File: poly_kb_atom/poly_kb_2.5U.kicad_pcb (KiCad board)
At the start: 2 copper layers, 47.6 x 19 mm, 46 parts, among them J1 Conn_01x16, J10 North2, J2 North, J3 WestFront, J4 EastFront, J5 WestBack, J6 EastBack, J7 South, J8 North2, J9 South2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

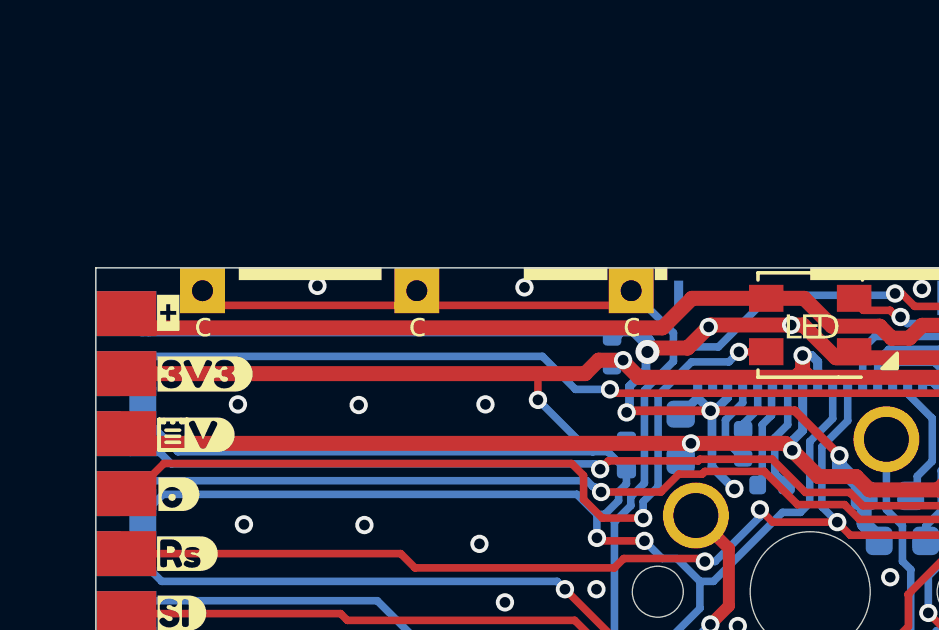
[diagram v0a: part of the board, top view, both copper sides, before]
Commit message: Added optional C7 and fix LED silkscreens
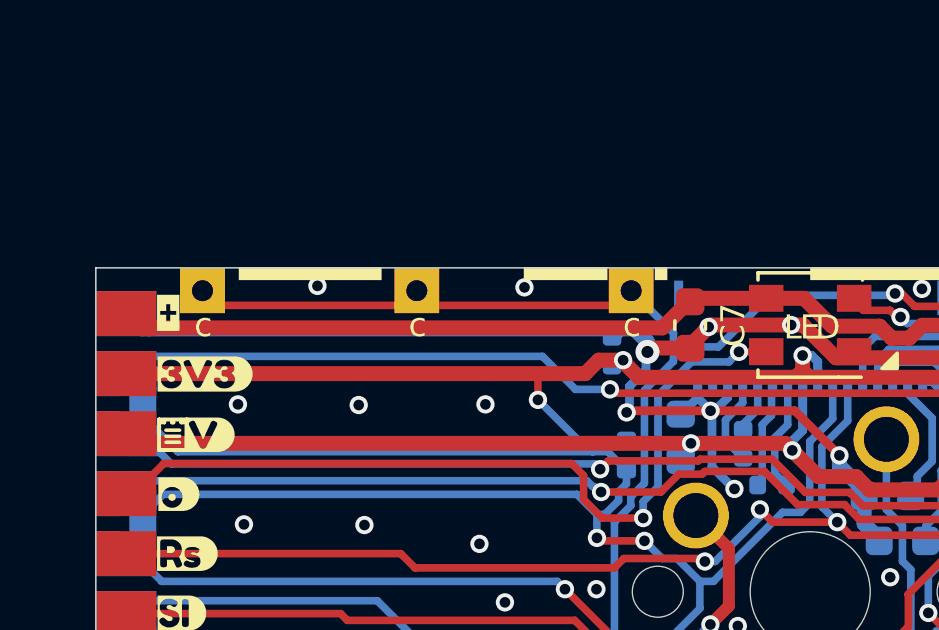
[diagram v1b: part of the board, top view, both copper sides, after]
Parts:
- removed the J10 at (81.5, 54.9)
- added C7: 100nF, Capacitor_SMD:C_0603_1608Metric, F.Cu at (97.7, 56.1)
- added J11: North2, poly_kb:TestPoin_1.5x1.5mm_Drill0.7mm, F.Cu at (81.5, 54.9)
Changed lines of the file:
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@@
       ) (layer "F.SilkS") (width 0) (fill solid))
+  )
+  (footprint "Capacitor_SMD:C_0603_1608Metric" (layer "F.Cu")
+    (at 97.7265 56.0578 -90)
+    (descr "Capacitor SMD 0603 (1608 Metric), square (rectangular) end terminal, IPC_7351 nominal, (Body size source: IPC-SM-782 page 76, https://www.pcb-3d.com/wordpress/wp-content/uploads/ipc-sm-782a_amendment_1_and_2.pdf), generated with kicad-footprint-generator")
+    (tags "capacitor")
+    (property "LCSC" "C19666")
+    (property "Sheetfile" "SSD1306_TO_SPI.kicad_sch")
+    (property "Sheetname" "sheet605ED2EB")
+    (attr smd)
+    (fp_text reference "C7" (at 0 -1.43 90) (layer "F.SilkS")
+      (effects (font (size 0.8 0.8) (thickness 0.15)))
+    )
+    (fp_text value "100nF" (at 0 1.43 90) (layer "F.Fab")
+      (effects (font (size 1 1) (thickness 0.15)))
+    )
+    (fp_text user "${REFERENCE}" (at 0 0 90) (layer "F.Fab")
+      (effects (font (size 0.4 0.4) (thickness 0.06)))
+    )
+    (fp_line (start -0.14058 0.51) (end 0.14058 0.51) (layer "F.SilkS") (width 0.12))
+    (fp_line (start -0.14058 -0.51) (end 0.14058 -0.51) (layer "F.SilkS") (width 0.12))
+    (fp_line (start -1.48 -0.73) (end 1.48 -0.73) (layer "F.CrtYd") (width 0.05))
+    (fp_line (start 1.48 -0.73) (end 1.48 0.73) (layer "F.CrtYd") (width 0.05))
+    (fp_line (start 1.48 0.73) (end -1.48 0.73) (layer "F.CrtYd") (width 0.05))
+    (fp_line (start -1.48 0.73) (end -1.48 -0.73) (layer "F.CrtYd") (width 0.05))
+    (fp_line (start -0.8 -0.4) (end 0.8 -0.4) (layer "F.Fab") (width 0.1))
+    (fp_line (start -0.8 0.4) (end -0.8 -0.4) (layer "F.Fab") (width 0.1))
+    (fp_line (start 0.8 0.4) (end -0.8 0.4) (layer "F.Fab") (width 0.1))
+    (fp_line (start 0.8 -0.4) (end 0.8 0.4) (layer "F.Fab") (width 0.1))
+    (pad "1" smd roundrect (at -0.775 0 270) (size 0.9 0.95) (layers "F.Cu" "F.Paste" "F.Mask") (roundrect_rratio 0.25)
+      (net 15 "/Keyboard/sheet605ED2EB/5V") (pintype "passive"))
+    (pad "2" smd roundrect (at 0.775 0 270) (size 0.9 0.95) (layers "F.Cu" "F.Paste" "F.Mask") (roundrect_rratio 0.25)
+      (net 1 "/Keyboard/sheet605ED2EB/GND") (pintype "passive"))
+    (model "${KICAD6_3DMODEL_DIR}/Capacitor_SMD.3dshapes/C_0603_1608Metric.wrl"
+      (offset (xyz 0 0 0))
+      (scale (xyz 1 1 1))
+      (rotate (xyz 0 0 0))
+    )
   )
   (footprint "kibuzzard-61EFD863" (layer "F.Cu")
@@
       ) (layer "F.SilkS") (width 0) (fill solid))
   )
-  (footprint "poly_kb:TestPoin_1.5x1.5mm_Drill0.7mm" (layer "F.Cu")
-    (at 81.47025 54.9148)
-    (descr "THT rectangular pad as test Point, square 1.5mm side length, hole diameter 0.7mm")
-    (tags "test point THT pad rectangle square")
-    (property "Sheetfile" "keyboard.kicad_sch")
-    (property "Sheetname" "Keyboard")
-    (attr exclude_from_pos_files)
-    (fp_text reference "J10" (at -1.143 0) (layer "F.SilkS") hide
-      (effects (font (size 0.8 0.8) (thickness 0.153)))
-    )
-    (fp_text value "North2" (at 0 -3.4417) (layer "F.Fab")
-      (effects (font (size 1 1) (thickness 0.15)))
-    )
-    (fp_text user "${REFERENCE}" (at 0 -1.65) (layer "F.Fab") hide
-      (effects (font (size 1 1) (thickness 0.15)))
-    )
-    (pad "1" thru_hole rect locked (at 0 0) (size 1.5 1.5) (drill 0.7) (layers *.Cu *.Mask)
-      (net 18 "/Keyboard/sheet605ED2EB/KeyCol") (pinfunction "Pin_1") (pintype "passive"))
-  )
   (footprint "kibuzzard-61EFDAEE" (layer "F.Cu")
     (at 80.966739 63.677507)
@@
         (xy -0.758349 -0.585258)
       ) (layer "F.SilkS") (width 0) (fill solid))
-  )
-  (footprint "poly_kb:TestPoin_1.5x1.5mm_Drill0.7mm" (layer "F.Cu")
-    (at 88.61425 54.9148)
-    (descr "THT rectangular pad as test Point, square 1.5mm side length, hole diameter 0.7mm")
-    (tags "test point THT pad rectangle square")
-    (property "Sheetfile" "keyboard.kicad_sch")
-    (property "Sheetname" "Keyboard")
-    (attr exclude_from_pos_files)
-    (fp_text reference "J10" (at -1.143 0) (layer "F.SilkS") hide
-      (effects (font (size 0.8 0.8) (thickness 0.153)))
-    )
-    (fp_text value "North2" (at 0 -3.4417) (layer "F.Fab")
-      (effects (font (size 1 1) (thickness 0.15)))
-    )
-    (fp_text user "${REFERENCE}" (at 0 -1.65) (layer "F.Fab") hide
-      (effects (font (size 1 1) (thickness 0.15)))
-    )
-    (pad "1" thru_hole rect locked (at 0 0) (size 1.5 1.5) (drill 0.7) (layers *.Cu *.Mask)
-      (net 18 "/Keyboard/sheet605ED2EB/KeyCol") (pinfunction "Pin_1") (pintype "passive"))
   )
   (footprint "kibuzzard-61EFABBF" (layer "F.Cu")
@@
     )
     (fp_text user "${REFERENCE}" (at 0 -1.65) (layer "F.Fab")
+      (effects (font (size 1 1) (thickness 0.15)))
+    )
+    (pad "1" thru_hole rect locked (at 0 0) (size 1.5 1.5) (drill 0.7) (layers *.Cu *.Mask)
+      (net 18 "/Keyboard/sheet605ED2EB/KeyCol") (pinfunction "Pin_1") (pintype "passive"))
+  )
+  (footprint "poly_kb:TestPoin_1.5x1.5mm_Drill0.7mm" (layer "F.Cu")
+    (at 81.4705 54.9148)
+    (descr "THT rectangular pad as test Point, square 1.5mm side length, hole diameter 0.7mm")
+    (tags "test point THT pad rectangle square")
+    (property "Sheetfile" "keyboard.kicad_sch")
+    (property "Sheetname" "Keyboard")
+    (attr exclude_from_pos_files)
+    (fp_text reference "J11" (at -1.143 0) (layer "F.SilkS") hide
+      (effects (font (size 0.8 0.8) (thickness 0.153)))
+    )
+    (fp_text value "North2" (at 0 -3.4417) (layer "F.Fab")
+      (effects (font (size 1 1) (thickness 0.15)))
+    )
+    (fp_text user "${REFERENCE}" (at 0 -1.65) (layer "F.Fab") hide
       (effects (font (size 1 1) (thickness 0.15)))
     )
@@
   )
   (footprint "poly_kb:TestPoin_1.5x1.5mm_Drill0.7mm" (layer "F.Cu")
+    (at 88.61425 54.9148)
+    (descr "THT rectangular pad as test Point, square 1.5mm side length, hole diameter 0.7mm")
+    (tags "test point THT pad rectangle square")
+    (property "Sheetfile" "keyboard.kicad_sch")
+    (property "Sheetname" "Keyboard")
+    (attr exclude_from_pos_files)
+    (fp_text reference "J10" (at -1.143 0) (layer "F.SilkS") hide
+      (effects (font (size 0.8 0.8) (thickness 0.153)))
+    )
+    (fp_text value "North2" (at 0 -3.4417) (layer "F.Fab")
+      (effects (font (size 1 1) (thickness 0.15)))
+    )
+    (fp_text user "${REFERENCE}" (at 0 -1.65) (layer "F.Fab") hide
+      (effects (font (size 1 1) (thickness 0.15)))
+    )
+    (pad "1" thru_hole rect locked (at 0 0) (size 1.5 1.5) (drill 0.7) (layers *.Cu *.Mask)
+      (net 18 "/Keyboard/sheet605ED2EB/KeyCol") (pinfunction "Pin_1") (pintype "passive"))
+  )
+  (footprint "poly_kb:TestPoin_1.5x1.5mm_Drill0.7mm" (layer "F.Cu")
